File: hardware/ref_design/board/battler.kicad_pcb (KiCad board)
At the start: 2 copper layers, 74.9 x 151.5 mm, 170 parts, among them J1 TYPE-C-31-M-12, J2 53261-0271, J3 FH12-50S-0.5SH(55), J4 SM02B-SRSS-TB, J7 DEBUG PADS, J8 DM3AT-SF-PEJM5, Q1 2N7002, Q3 2N7002, Q5 AO3400A, Q6 AO3400A, SW1 P1 UP, SW10 P2 DOWN, SW11 P2 LEFT, SW12 P2 RIGHT, SW13 P2 A, SW14 P2 B, SW15 P2 X, SW16 P2 Y, SW2 P1 DOWN, SW20 P1 SELECT, SW21 P1 START, SW22 P2 SELECT, SW23 P2 START, SW24 POWER, SW3 P1 LEFT, SW4 P1 RIGHT, SW5 P1 A, SW6 P1 B, SW7 P1 X, SW8 P1 Y, SW9 P2 UP, U1 SRV05-4, U10 MCP6001, U11 SN74HC165PWR, U2 BQ24073RGTR, U3 TLV75733PDBVR, U4 ESP32-S3-WROOM-1U-N16R8, U6 MCP6002, U7 FM8002A, U8 SN74HC165PWR, U9 SN74HC165PWR

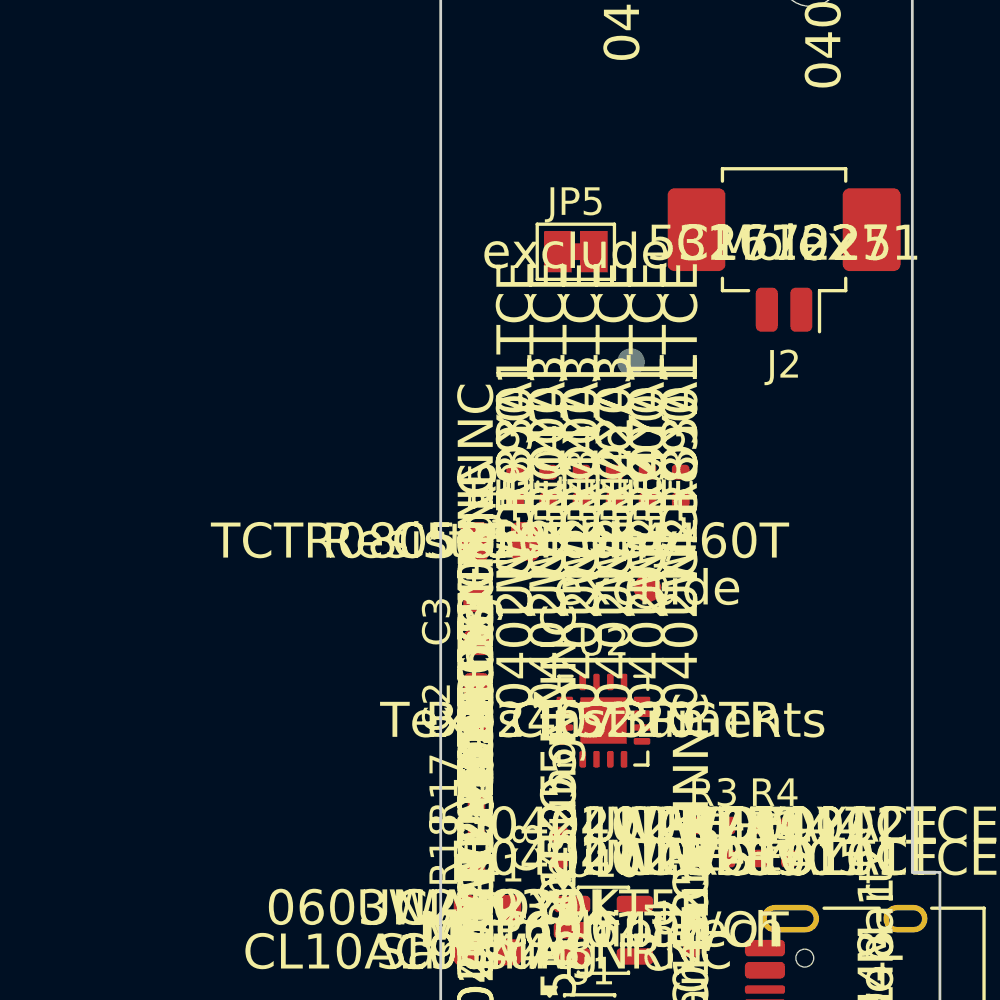
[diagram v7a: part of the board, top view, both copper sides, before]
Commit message: ref_design ESP32-S3: TH1 back at the hole's right edge (120.2, 79.0)
Co-Authored-By: Claude Sonnet 5.5 <noreply@anthropic.com>
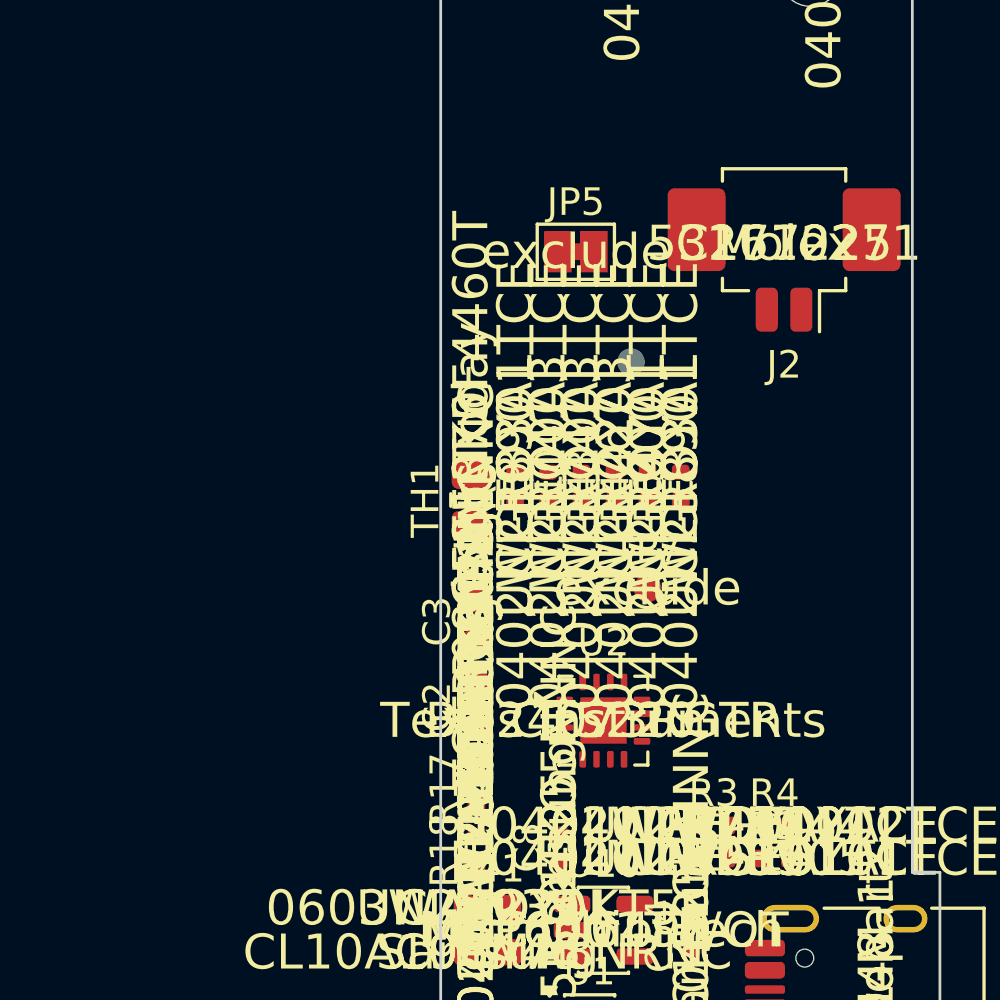
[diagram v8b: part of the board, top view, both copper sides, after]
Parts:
- moved TH1 1.83 mm to (120.2, 79.0), turned to 90 degrees
